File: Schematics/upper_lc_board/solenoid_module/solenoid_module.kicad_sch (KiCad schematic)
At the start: 16 parts

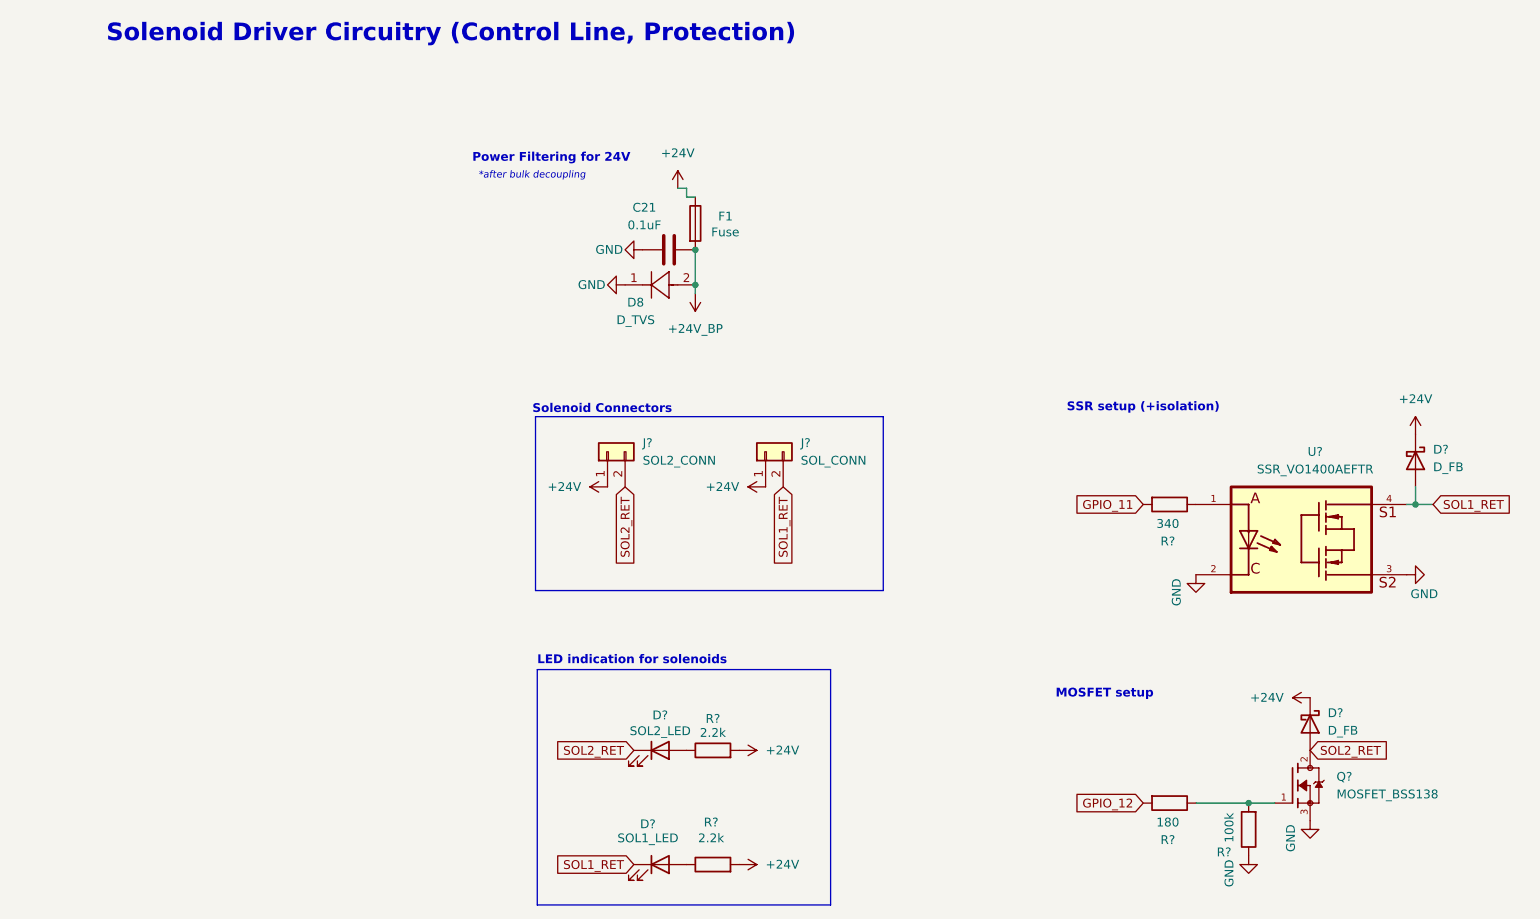
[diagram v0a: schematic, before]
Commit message: revise & organize some circuitry, next: replace MUX with ideal diodes, finish layout, rename GPIO labels for clarity
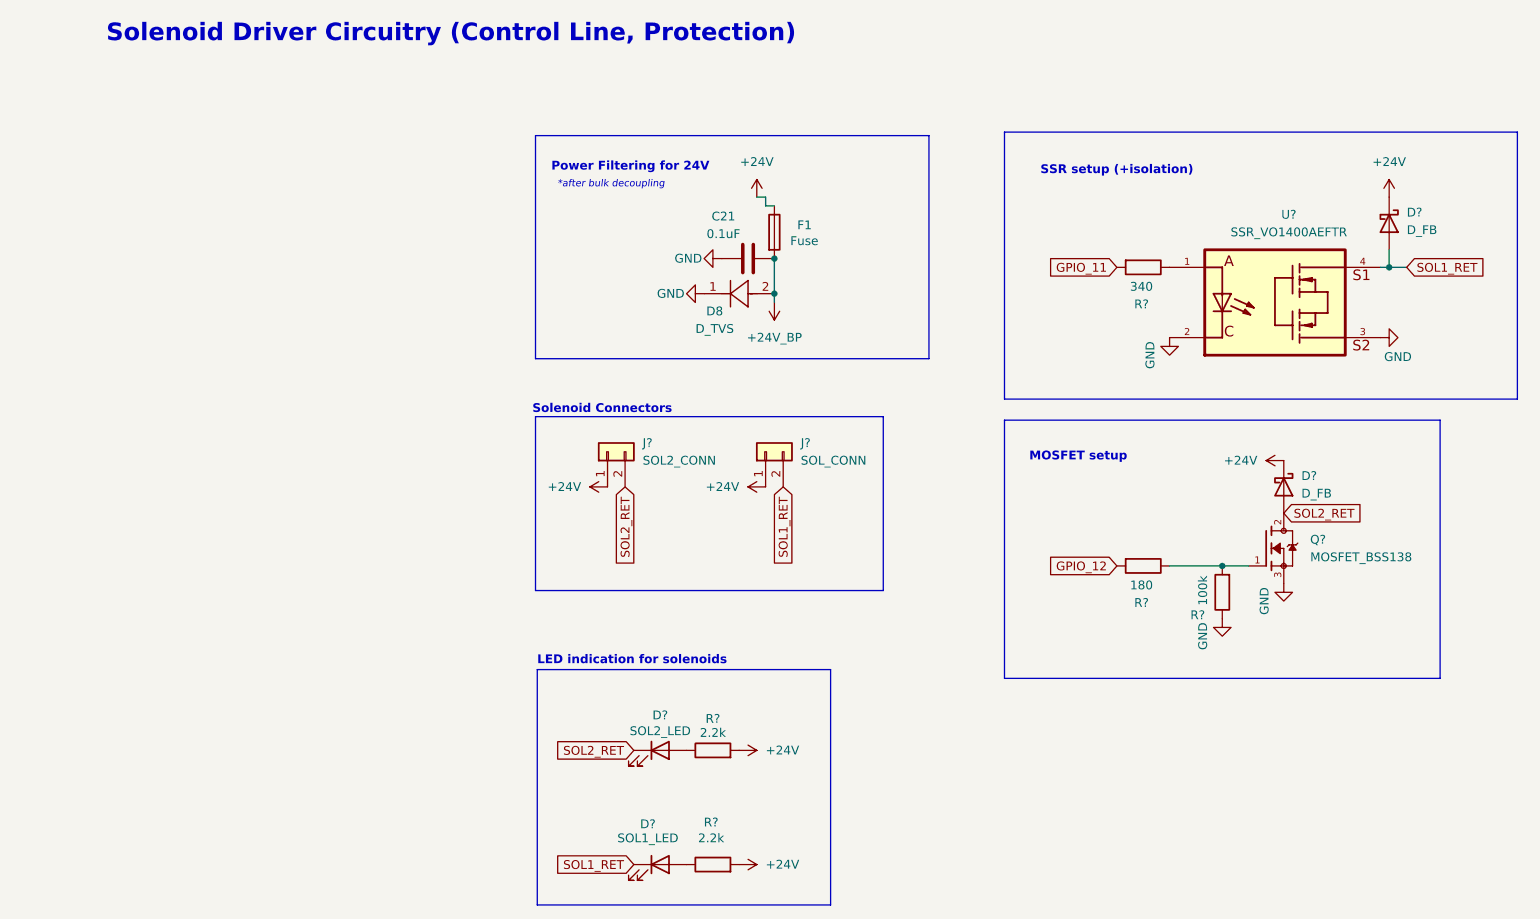
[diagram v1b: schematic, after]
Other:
- moved on the sheet: C21, D8, D?, F1, Q?, R?, U?

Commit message: add vertical connectors, revert MUX circuitry to ORing setup w ideal diodes
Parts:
- J? (x2): footprint 530480210:MOLEX_530480210 -> CONNS:CONN02_530470260_MOL
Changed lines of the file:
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@@
 			)
 		)
-		(property "Footprint" "530480210:MOLEX_530480210"
+		(property "Footprint" "CONNS:CONN02_530470260_MOL"
 			(at 110.49 82.55 0)
 			(effects
@@
 			)
 		)
-		(property "Footprint" "530480210:MOLEX_530480210"
+		(property "Footprint" "CONNS:CONN02_530470260_MOL"
 			(at 87.63 82.55 0)
 			(effects

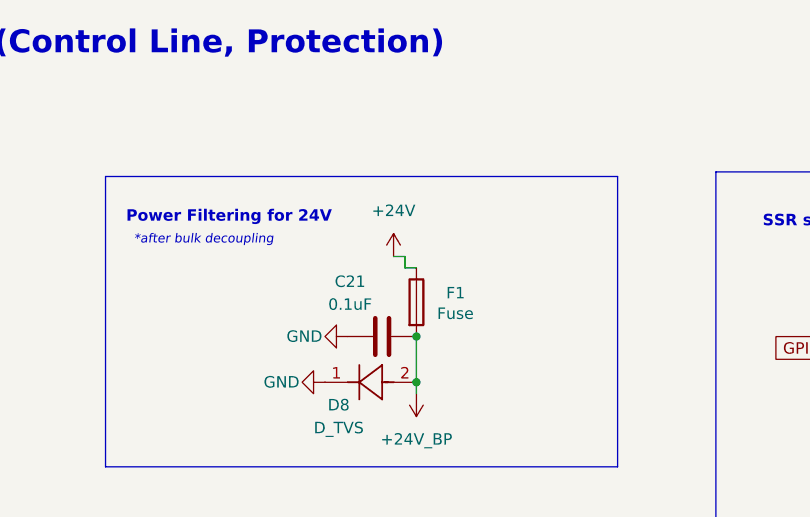
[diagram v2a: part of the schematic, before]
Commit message: add thermistor circuitry & update layout
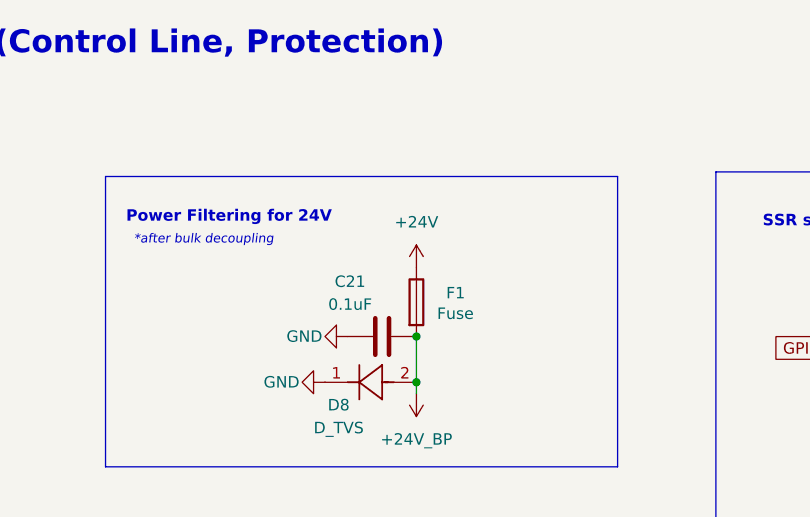
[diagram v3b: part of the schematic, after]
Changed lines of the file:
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@@
-	(wire
-		(pts
-			(xy 111.76 46.99) (xy 110.49 46.99)
-		)
-		(stroke
-			(width 0)
-			(type default)
-		)
-	)
 	(wire
 		(pts
@@
 	(wire
 		(pts
-			(xy 110.49 46.99) (xy 110.49 45.72)
+			(xy 168.91 99.06) (xy 176.53 99.06)
 		)
 		(stroke
@@
 	(wire
 		(pts
-			(xy 168.91 99.06) (xy 176.53 99.06)
-		)
-		(stroke
-			(width 0)
-			(type default)
-		)
-	)
-	(wire
-		(pts
 			(xy 199.39 55.88) (xy 200.66 55.88)
-		)
-		(stroke
-			(width 0)
-			(type default)
-		)
-	)
-	(wire
-		(pts
-			(xy 110.49 45.72) (xy 109.22 45.72)
 		)
 		(stroke
@@
 	(symbol
 		(lib_id "power:+24V")
-		(at 109.22 45.72 0)
+		(at 111.76 46.99 0)
 		(unit 1)
 		(exclude_from_sim no)
@@
 		(fields_autoplaced yes)
 		(property "Reference" "#PWR082"
-			(at 109.22 49.53 0)
+			(at 111.76 50.8 0)
 			(effects
 				(font
@@
 		)
 		(property "Value" "+24V"
-			(at 109.22 40.64 0)
+			(at 111.76 41.91 0)
 			(effects
 				(font
@@
 		)
 		(property "Footprint" ""
-			(at 109.22 45.72 0)
+			(at 111.76 46.99 0)
 			(effects
 				(font
@@
 		)
 		(property "Datasheet" ""
-			(at 109.22 45.72 0)
+			(at 111.76 46.99 0)
 			(effects
 				(font
@@
 		)
 		(property "Description" "Power symbol creates a global label with name \"+24V\""
-			(at 109.22 45.72 0)
-			(effects
-				(font
+			(at 111.76 46.99 0)
+			(effects
+				(font

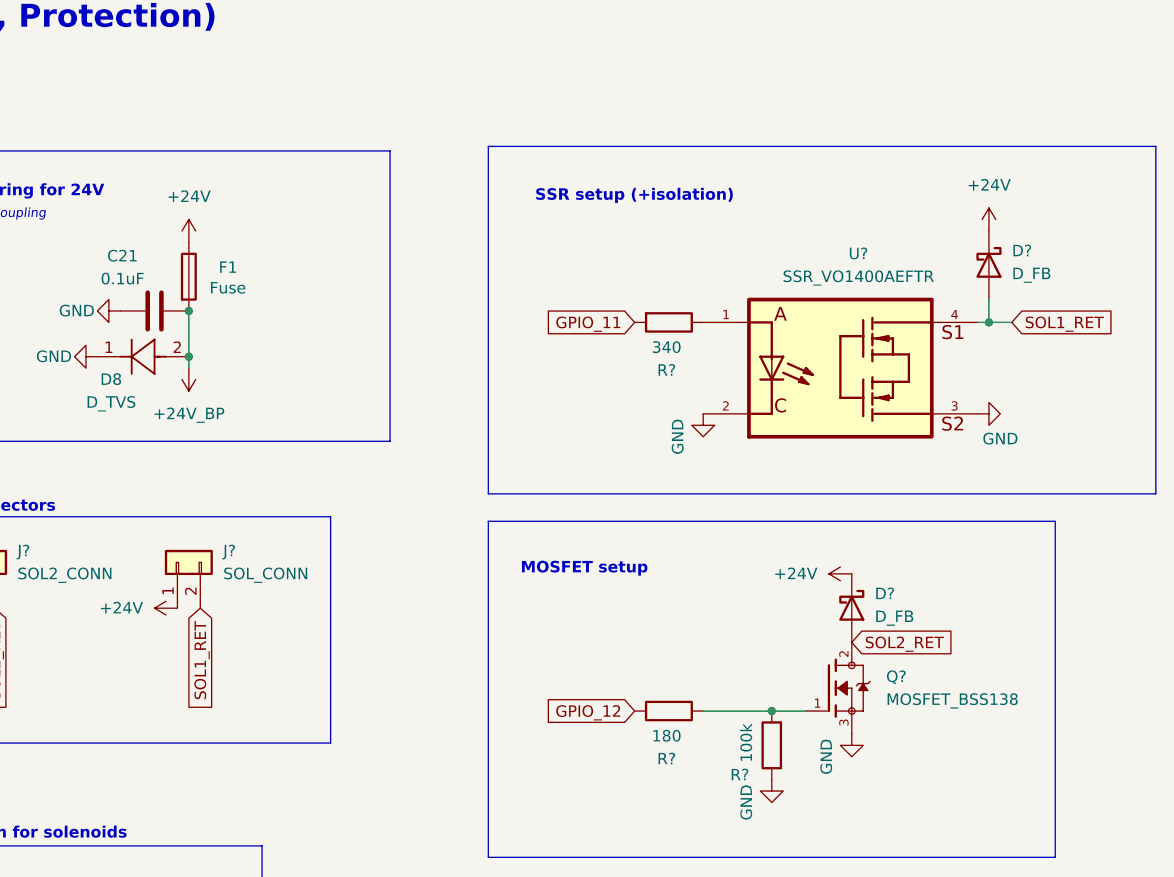
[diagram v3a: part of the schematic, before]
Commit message: add testing points throughout board schematic
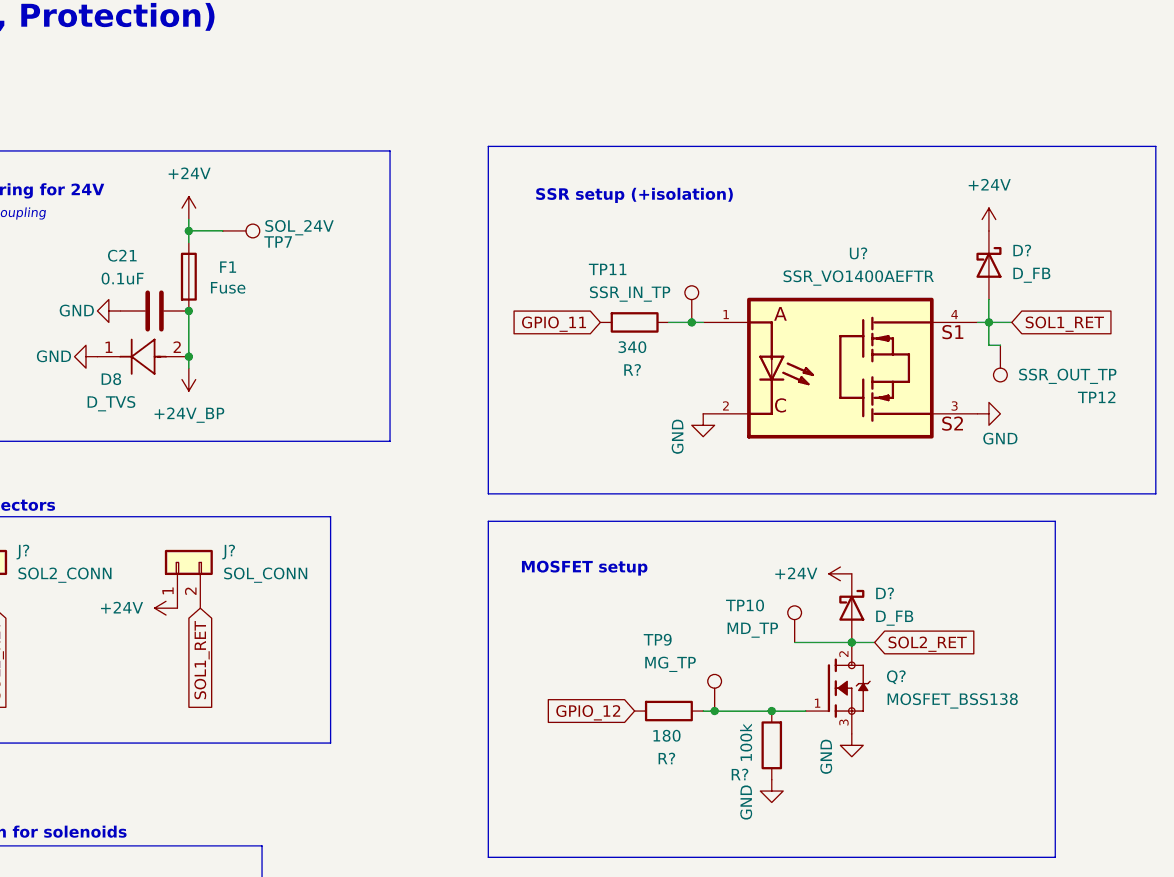
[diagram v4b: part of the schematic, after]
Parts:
- added TP10: MD_TP, TestPoint:TestPoint_Pad_1.0x1.0mm, symbol Connector:TestPoint
- added TP11: SSR_IN_TP, TestPoint:TestPoint_Pad_1.0x1.0mm, symbol Connector:TestPoint
- added TP12: SSR_OUT_TP, TestPoint:TestPoint_Pad_1.0x1.0mm, symbol Connector:TestPoint
- added TP7: SOL_24V, TestPoint:TestPoint_Pad_1.0x1.0mm, symbol Connector:TestPoint
- added TP9: MG_TP, TestPoint:TestPoint_Pad_1.0x1.0mm, symbol Connector:TestPoint
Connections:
- net +24V: now also TP7.1
- net SOL1_RET: now also TP12.1
- net SOL2_RET: now also TP10.1
- net at Q?.1, R?.1, R?.2: now also TP9.1
- net at R?.1, U?.1: now also TP11.1
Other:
- moved on the sheet: R?

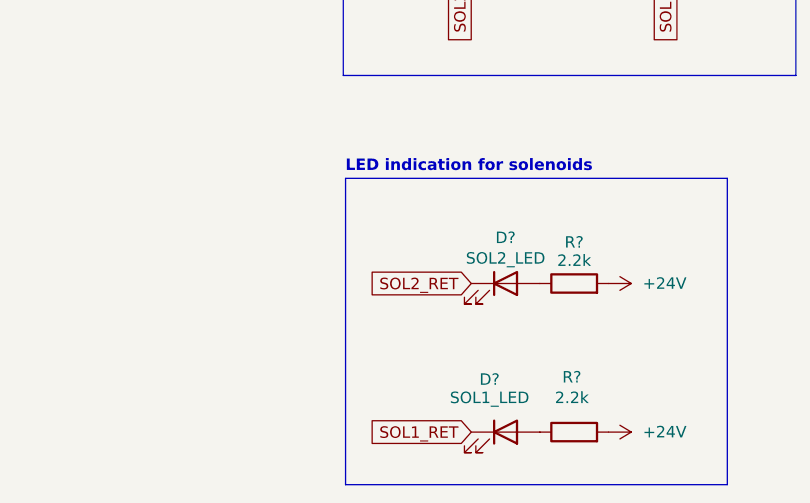
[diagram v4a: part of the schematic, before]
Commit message: fix shunt resistor, add test point to layout
- sync issue with backplane connector footprint
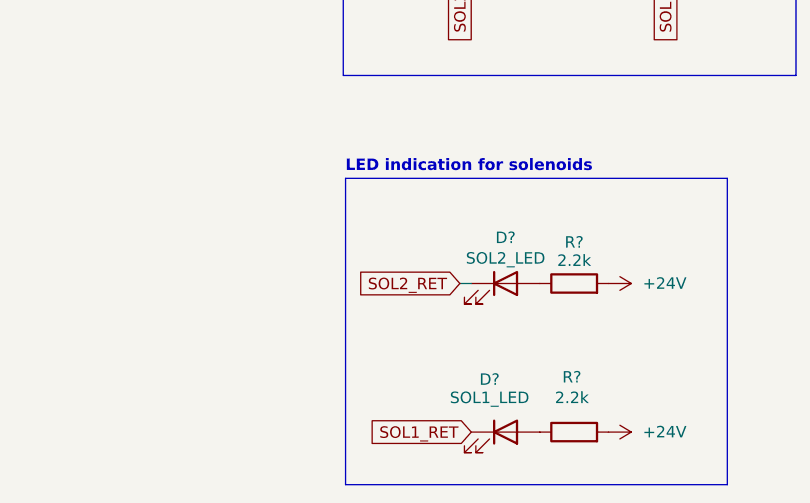
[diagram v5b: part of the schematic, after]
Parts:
- TP10, TP11, TP12, TP7, TP9: footprint TestPoint:TestPoint_Pad_1.0x1.0mm -> TestPoint:TestPoint_Pad_D1.0mm
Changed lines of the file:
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@@
+	(wire
+		(pts
+			(xy 90.17 125.73) (xy 91.44 125.73)
+		)
+		(stroke
+			(width 0)
+			(type default)
+		)
+	)
 	(wire
 		(pts
@@
 	(global_label "SOL2_RET"
 		(shape input)
-		(at 91.44 125.73 180)
+		(at 90.17 125.73 180)
 		(fields_autoplaced yes)
 		(effects
@@
 		)
 		(property "Intersheetrefs" "${INTERSHEET_REFS}"
-			(at 79.323 125.73 0)
+			(at 78.053 125.73 0)
 			(effects
 				(font
@@
 			)
 		)
-		(property "Footprint" "TestPoint:TestPoint_Pad_1.0x1.0mm"
+		(property "Footprint" "TestPoint:TestPoint_Pad_D1.0mm"
 			(at 196.85 58.42 0)
 			(effects
@@
 			)
 		)
-		(property "Footprint" "TestPoint:TestPoint_Pad_1.0x1.0mm"
+		(property "Footprint" "TestPoint:TestPoint_Pad_D1.0mm"
 			(at 184.15 91.44 0)
 			(effects
@@
 			)
 		)
-		(property "Footprint" "TestPoint:TestPoint_Pad_1.0x1.0mm"
+		(property "Footprint" "TestPoint:TestPoint_Pad_D1.0mm"
 			(at 172.72 55.88 0)
 			(effects
@@
 			)
 		)
-		(property "Footprint" "TestPoint:TestPoint_Pad_1.0x1.0mm"
+		(property "Footprint" "TestPoint:TestPoint_Pad_D1.0mm"
 			(at 115.57 50.8 0)
 			(effects
@@
 			)
 		)
-		(property "Footprint" "TestPoint:TestPoint_Pad_1.0x1.0mm"
+		(property "Footprint" "TestPoint:TestPoint_Pad_D1.0mm"
 			(at 175.26 99.06 0)
 			(effects

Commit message: routing work
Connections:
- net GPIO_11: now also R?.2; no longer R?.2
- net GPIO_12: now also R?.2; no longer R?.2
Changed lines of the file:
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@@
 	(global_label "GPIO_11"
-		(shape input)
-		(at 157.48 55.88 180)
-		(fields_autoplaced yes)
-		(effects
-			(font
-				(size 1.27 1.27)
-			)
-			(justify right)
-		)
-		(property "Intersheetrefs" "${INTERSHEET_REFS}"
-			(at 146.6329 55.88 0)
-			(effects
-				(font
-					(size 1.27 1.27)
-				)
-				(justify right)
-				(hide yes)
-			)
-		)
-	)
-	(global_label "GPIO_12"
 		(shape input)
 		(at 161.29 99.06 180)
@@
 			(effects
 				(font
+					(size 1.27 1.27)
+				)
+				(justify right)
+				(hide yes)
+			)
+		)
+	)
+	(global_label "GPIO_12"
+		(shape input)
+		(at 157.48 55.88 180)
+		(fields_autoplaced yes)
+		(effects
+			(font
+				(size 1.27 1.27)
+			)
+			(justify right)
+		)
+		(property "Intersheetrefs" "${INTERSHEET_REFS}"
+			(at 146.6329 55.88 0)
+			(effects
+				(font
